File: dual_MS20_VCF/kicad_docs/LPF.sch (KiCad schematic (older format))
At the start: 30 parts, among them Q3 BC558, Q4 BC558, U4 LM13700, U5 MC1458, U6 MC1458

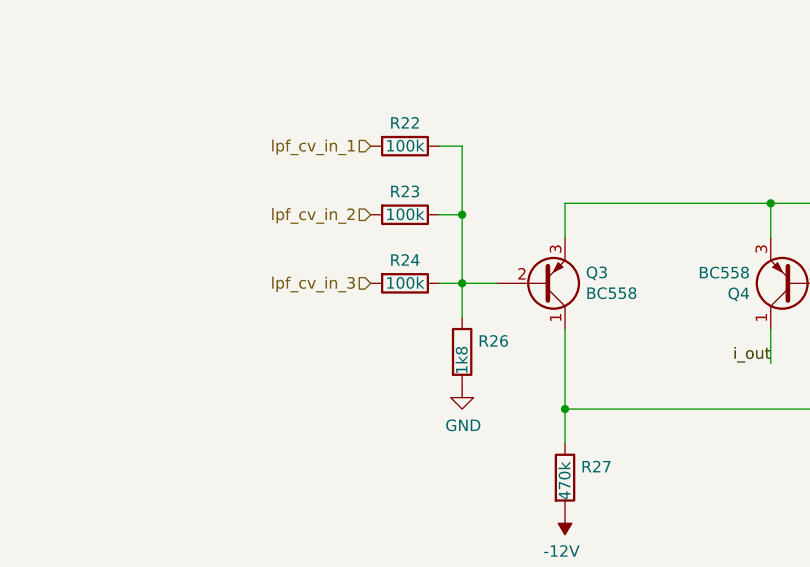
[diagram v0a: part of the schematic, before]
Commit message: change scaling resistors for manual cutoff controls
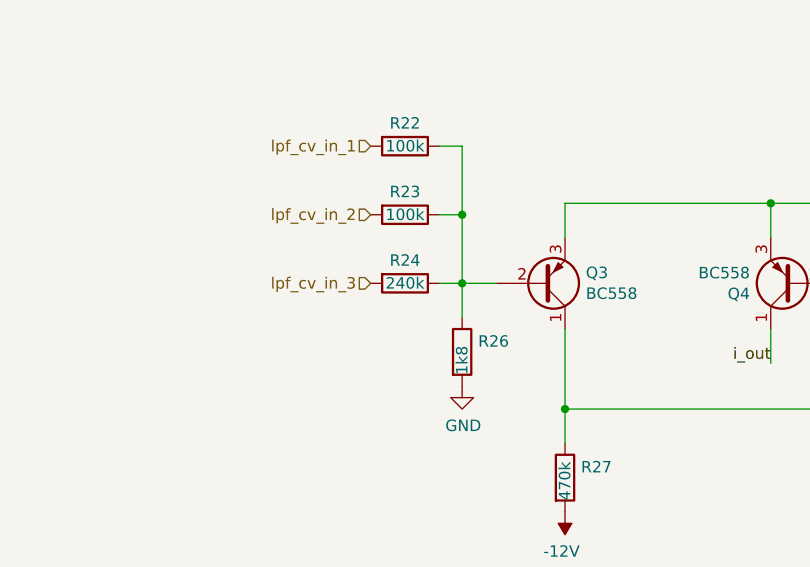
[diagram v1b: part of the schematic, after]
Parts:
- R24: value 100k -> 240k
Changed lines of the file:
@@
 AR Path="/5EFEDA66/5F01D142" Ref="R24"  Part="1"
 F 0 "R24" V 2800 6350 50  0000 C CNN
-F 1 "100k" V 2900 6350 50  0000 C CNN
+F 1 "240k" V 2900 6350 50  0000 C CNN
 F 2 "Resistor_THT:R_Axial_DIN0207_L6.3mm_D2.5mm_P10.16mm_Horizontal" V 2830 6350 50  0001 C CNN
 F 3 "~" H 2900 6350 50  0001 C CNN
